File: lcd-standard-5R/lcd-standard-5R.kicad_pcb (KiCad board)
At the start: 2 copper layers, 137.4 x 82.6 mm, 114 parts, among them J1 SWD, J2 Conn_01x40_MountingPin, J3 Micro_SD_Card_Det1, J4 USB_C_Receptacle_USB2.0_16P, J5 Conn_01x06_MountingPin, J6 Serial, J7 Conn_ARM_JTAG_SWD_10, J8 Conn_01x02_MountingPin, J9 Conn_01x10_MountingPin, Q1 DMG2301L, Q2 MMBT3904, Q3 MMBT3904, Q4 MMBT3904, SW1 BOOT0, SW2 RST, U1 MAX98357A, U2 TPS61169, U3 XPT2046TS, U4 CAT24C256, U5 AMS1117-3.3, U6 siplex-som-s16

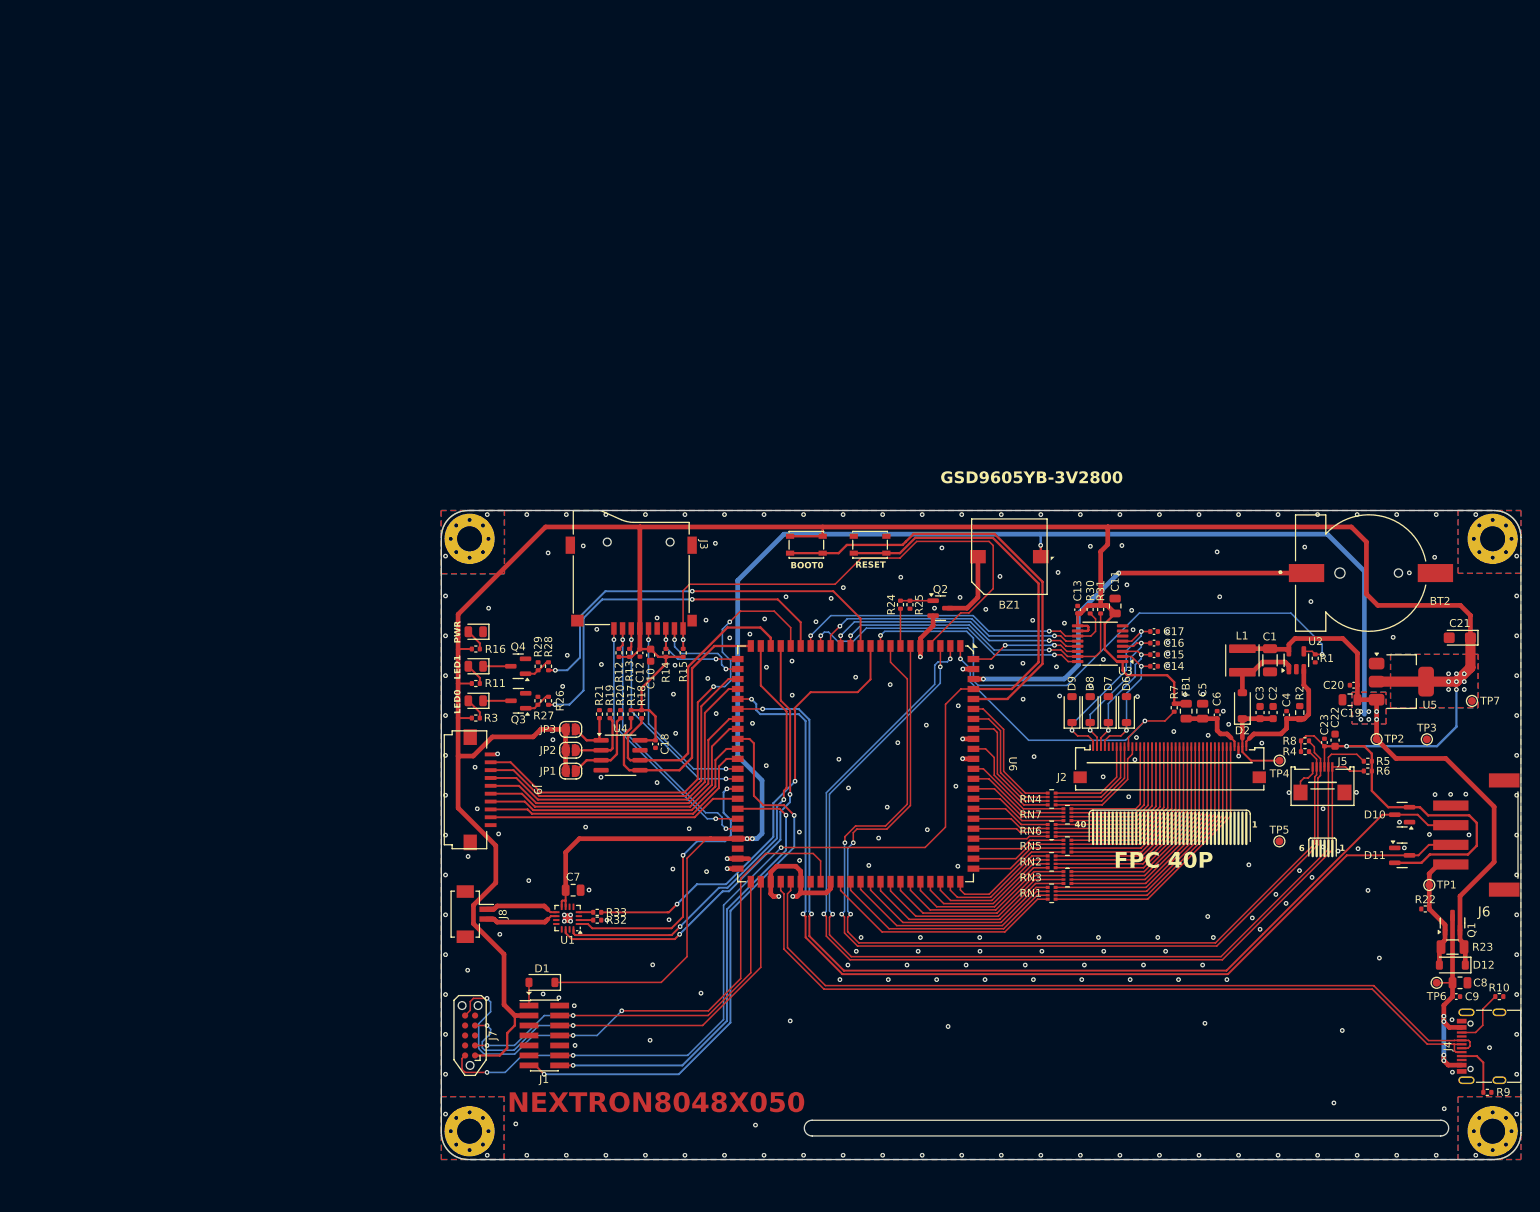
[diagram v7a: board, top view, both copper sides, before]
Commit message: Change LCD 5R to onboard MCU, cause separate boards are too expensive
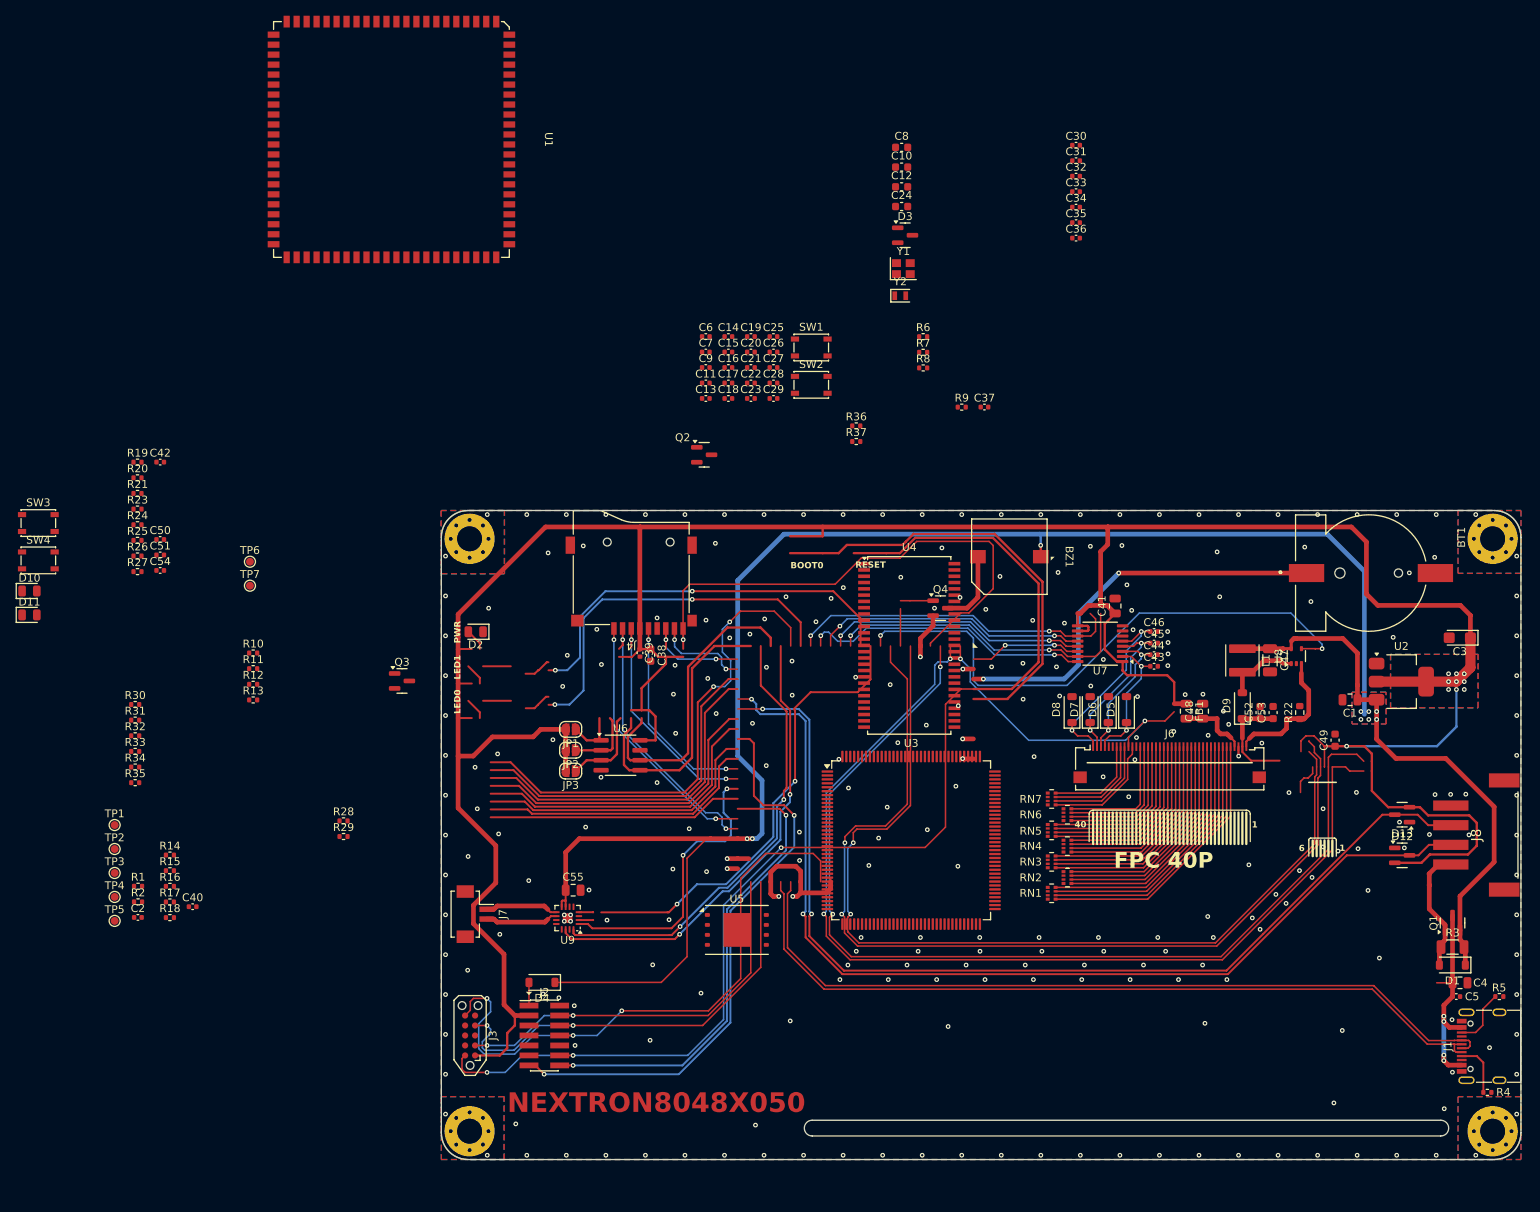
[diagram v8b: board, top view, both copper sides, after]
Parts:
- removed BT2: S8411-45R, CR1220-Batt-conn-S8411-45R:CR1220-Batt-conn-S8411-45R
- removed the C4 at (184.0, 79.9)
- removed the C5 at (173.3, 79.5)
- removed the J1 at (89.5, 120.7)
- removed J5: Conn_01x06_MountingPin, Connector_FPC:Conn_FPC_6P_0.5mm_XUNPU_FPC-05FB-6PH20
- removed J9: Conn_01x10_MountingPin, Connector_FPC:Conn_FPC_10P_1mm_G-SWITCH_GT-F1008SR20-10SMT01
- removed the R4 at (186.3, 84.6)
- removed the R5 at (194.3, 85.8)
- removed the U1 at (92.5, 105.8)
- added BT1: S8411-45R, CR1220-Batt-conn-S8411-45R:CR1220-Batt-conn-S8411-45R, F.Cu at (194.5, 61.9)
- added C24: 4u7, Capacitor_SMD:C_0603_1608Metric, F.Cu at (135.0, 15.2)
- added C25: 16p, Capacitor_SMD:C_0402_1005Metric, F.Cu at (118.7, 31.8)
- added C26: 16p, Capacitor_SMD:C_0402_1005Metric, F.Cu at (118.7, 33.7)
- added C27: 10p, Capacitor_SMD:C_0402_1005Metric, F.Cu at (118.7, 35.7)
- added C28: 10p, Capacitor_SMD:C_0402_1005Metric, F.Cu at (118.7, 37.7)
- added C29: 100n, Capacitor_SMD:C_0402_1005Metric, F.Cu at (118.7, 39.7)
- added C30: 100n, Capacitor_SMD:C_0402_1005Metric, F.Cu at (157.2, 7.43)
- added C31: 100n, Capacitor_SMD:C_0402_1005Metric, F.Cu at (157.2, 9.40)
- added C32: 100n, Capacitor_SMD:C_0402_1005Metric, F.Cu at (157.2, 11.4)
- added C33: 100n, Capacitor_SMD:C_0402_1005Metric, F.Cu at (157.2, 13.3)
- added C34: 100n, Capacitor_SMD:C_0402_1005Metric, F.Cu at (157.2, 15.3)
- added C35: 100n, Capacitor_SMD:C_0402_1005Metric, F.Cu at (157.2, 17.3)
- added C36: 100n, Capacitor_SMD:C_0402_1005Metric, F.Cu at (157.2, 19.2)
- added C37: 100n, Capacitor_SMD:C_0402_1005Metric, F.Cu at (145.5, 40.7)
- added C38: 1u, Capacitor_SMD:C_0603_1608Metric, F.Cu at (103.1, 72.3)
- added C39: 100n, Capacitor_SMD:C_0402_1005Metric, F.Cu at (101.7, 72.0)
- added C40: 100n, Capacitor_SMD:C_0402_1005Metric, F.Cu at (44.8, 104.3)
- added C41: 10u, Capacitor_SMD:C_0805_2012Metric, F.Cu at (162.2, 66.1)
- added C42: 100n, Capacitor_SMD:C_0402_1005Metric, F.Cu at (40.7, 47.8)
- added C43: 100n, Capacitor_SMD:C_0402_1005Metric, F.Cu at (167.1, 73.7)
- added C44: 100n, Capacitor_SMD:C_0402_1005Metric, F.Cu at (167.1, 72.3)
- added C45: 100n, Capacitor_SMD:C_0402_1005Metric, F.Cu at (167.1, 70.8)
- added C46: 100n, Capacitor_SMD:C_0402_1005Metric, F.Cu at (167.1, 69.3)
- added C47: 10u/1206, Capacitor_SMD:C_1206_3216Metric, F.Cu at (181.9, 73.0)
- added C48: 10u, Capacitor_SMD:C_0805_2012Metric, F.Cu at (173.3, 79.5)
- added C49: 1u, Capacitor_SMD:C_0603_1608Metric, F.Cu at (190.2, 83.1)
- added C50: 100n, Capacitor_SMD:C_0402_1005Metric, F.Cu at (40.7, 57.6)
- added C51: 100n, Capacitor_SMD:C_0402_1005Metric, F.Cu at (40.7, 59.6)
- added C52: 1u, Capacitor_SMD:C_0603_1608Metric, F.Cu at (180.6, 79.6)
- added C53: 1u, Capacitor_SMD:C_0603_1608Metric, F.Cu at (182.3, 79.6)
- added C54: 100n, Capacitor_SMD:C_0402_1005Metric, F.Cu at (40.7, 61.5)
- added C55: 10u, Capacitor_SMD:C_0805_2012Metric, F.Cu at (93.2, 102.2)
- added C8: 1u, Capacitor_SMD:C_0603_1608Metric, F.Cu at (135.0, 7.70)
- added C9: 100n, Capacitor_SMD:C_0402_1005Metric, F.Cu at (110.1, 35.7)
- added D13: BAT54S, Package_TO_SOT_SMD:SOT-23, F.Cu at (198.7, 92.6)
- added J4: Micro_SD_Card_Det1, TF-115:SD-TF-115, F.Cu at (100.6, 63.7)
- added R10: 10K, Resistor_SMD:R_0402_1005Metric, F.Cu at (52.5, 72.1)
- added R34: 10K, Resistor_SMD:R_0402_1005Metric, F.Cu at (37.5, 86.6)
- added R35: 2K, Resistor_SMD:R_0402_1005Metric, F.Cu at (37.5, 88.6)
- added R36: 1K, Resistor_SMD:R_0402_1005Metric, F.Cu at (129.2, 43.1)
- added R37: 10K, Resistor_SMD:R_0402_1005Metric, F.Cu at (129.2, 45.1)
- added R9: 10K, Resistor_SMD:R_0402_1005Metric, F.Cu at (142.7, 40.8)
- added SW3: BOOT0, Button_Switch_SMD:SW_SPST_PTS810, F.Cu at (25.1, 55.5)
- added SW4: RST, Button_Switch_SMD:SW_SPST_PTS810, F.Cu at (25.1, 60.3)
- added U6: CAT24C256, Package_SO:SOIC-8_3.9x4.9mm_P1.27mm, F.Cu at (99.2, 85.1)
- added U7: XPT2046TS, Package_SO:TSSOP-16_4.4x5mm_P0.65mm, F.Cu at (160.3, 70.9)
- added U8: TPS61169, Package_TO_SOT_SMD:SOT-353_SC-70-5, F.Cu at (185.2, 72.4)
- added U9: MAX98357A, Package_DFN_QFN:TQFN-16-1EP_3x3mm_P0.5mm_EP1.23x1.23mm, F.Cu at (92.5, 105.8)
- added Y1: 25MHz, Crystal:Crystal_SMD_2520-4Pin_2.5x2.0mm, F.Cu at (135.2, 23.1)
- added Y2: 32.768KHz, Crystal:Crystal_SMD_2012-2Pin_2.0x1.2mm, F.Cu at (134.8, 26.6)
- C1: value 10u/1206 -> 10u; footprint Capacitor_SMD:C_1206_3216Metric -> Capacitor_SMD:C_0805_2012Metric
- C10: value 1u -> 2u2
- C11, C19, C7: value 10u -> 100n; footprint Capacitor_SMD:C_0805_2012Metric -> Capacitor_SMD:C_0402_1005Metric
- C12: value 100n -> 2u2; footprint Capacitor_SMD:C_0402_1005Metric -> Capacitor_SMD:C_0603_1608Metric
- C2, C22: value 1u -> 100n; footprint Capacitor_SMD:C_0603_1608Metric -> Capacitor_SMD:C_0402_1005Metric
- C21: value 22uF -> 100n; footprint Capacitor_Tantalum_SMD:CP_EIA-3216-18_Kemet-A -> Capacitor_SMD:C_0402_1005Metric
- C3: value 1u -> 10uF; footprint Capacitor_SMD:C_0603_1608Metric -> Capacitor_Tantalum_SMD:CP_EIA-3216-18_Kemet-A
- D1: value NSR0320MW2T1G -> B5819W
- D10, D11: value BAT54S -> RED; footprint Package_TO_SOT_SMD:SOT-23 -> LED_SMD:LED_0805_2012Metric
- D12: value MBR0540 -> BAT54S; footprint Diode_SMD:D_SOD-123 -> Package_TO_SOT_SMD:SOT-23
- D2: value MBR0540 -> GREEN; footprint Diode_SMD:D_SOD-123 -> LED_SMD:LED_0805_2012Metric
- D3: value LED -> BAT54CW; footprint LED_SMD:LED_0805_2012Metric -> Package_TO_SOT_SMD:SOT-23
- D4: value LED -> B5819WS; footprint LED_SMD:LED_0805_2012Metric -> Diode_SMD:D_SOD-123
- D5: value LED -> MMSZ5226BT1G; footprint LED_SMD:LED_0805_2012Metric -> Diode_SMD:D_SOD-123
- D9: value MMSZ5226BT1G -> MBR0540
- J2: value Conn_01x40_MountingPin -> SWD; footprint Connector_FFC-FPC:Omron_XF2M-4015-1A_1x40-1MP_P0.5mm_Horizontal -> Connector_PinHeader_1.27mm:PinHeader_2x07_P1.27mm_Vertical_SMD
- J3: value Micro_SD_Card_Det1 -> Conn_ARM_JTAG_SWD_10; footprint TF-115:SD-TF-115 -> Connector:Tag-Connect_TC2050-IDC-NL_2x05_P1.27mm_Vertical
- J6: value Serial -> Conn_01x40_MountingPin; footprint S4B-XH-SM4-TB_LF__SN:S4BXHSM4TBLFSN -> Connector_FFC-FPC:Omron_XF2M-4015-1A_1x40-1MP_P0.5mm_Horizontal
- J7: value Conn_ARM_JTAG_SWD_10 -> Conn_01x02_MountingPin; footprint Connector:Tag-Connect_TC2050-IDC-NL_2x05_P1.27mm_Vertical -> Connector_Hirose:Hirose_DF13C_CL535-0402-2-51_1x02-1MP_P1.25mm_Vertical
- J8: value Conn_01x02_MountingPin -> Serial; footprint Connector_Hirose:Hirose_DF13C_CL535-0402-2-51_1x02-1MP_P1.25mm_Vertical -> S4B-XH-SM4-TB_LF__SN:S4BXHSM4TBLFSN
- L1: value 6.8u -> 4.7u
- Q1: value DMG2301L -> DMG3415
- R11: value 2K -> 10K
- R14, R15, R25: value 10K -> 2K2
- R16: value 2K -> 2K2
- R19, R20, R21, R6: value 2K2 -> 10K
- R2: value 4.7R -> 2K; footprint Resistor_SMD:R_0603_1608Metric -> Resistor_SMD:R_0402_1005Metric
- R22: value 10K -> 4.7R; footprint Resistor_SMD:R_0402_1005Metric -> Resistor_SMD:R_0603_1608Metric
- R23: value 0 -> 10K; footprint Resistor_SMD:R_1206_3216Metric -> Resistor_SMD:R_0402_1005Metric
- R24: value 1K -> 10K
- R26: value 1K -> 2K2
- R28: value 1K -> 1M
- R29: value 10K -> 100K
- R3: value 2K -> 0; footprint Resistor_SMD:R_0402_1005Metric -> Resistor_SMD:R_1206_3216Metric
- R30: value 10K -> 1K
- R32: value 100K -> 2K
- R33: value 1M -> 1K
- SW1: value BOOT0 -> SW_Push
- SW2: value RST -> SW_Push
- U2: value TPS61169 -> AMS1117-3.3; footprint Package_TO_SOT_SMD:SOT-23-5 -> Package_TO_SOT_SMD:SOT-223-3_TabPin2
- U3: value XPT2046TS -> STM32H743ZITx; footprint Package_SO:TSSOP-16_4.4x5mm_P0.65mm -> Package_QFP:LQFP-144_20x20mm_P0.5mm
- U4: value CAT24C256 -> MT48LC16M16A2P; footprint Package_SO:SOIC-8_3.9x4.9mm_P1.27mm -> Package_SO:TSOP-II-54_22.2x10.16mm_P0.8mm
- U5: value AMS1117-3.3 -> MT25Q; footprint Package_TO_SOT_SMD:SOT-223-3_TabPin2 -> Package_SON:WSON-8-1EP_8x6mm_P1.27mm_EP3.4x4.3mm
- moved D11 177.4 mm to (24.0, 67.2)
- moved D10 177.0 mm to (24.0, 64.2), turned to 0 degrees
- moved R23 176.4 mm to (37.8, 53.7)
- moved TP3 167.9 mm to (34.9, 100.0)
- moved TP1 167.5 mm to (34.9, 93.9)
- moved TP2 161.2 mm to (34.9, 97.0)
- moved TP6 160.3 mm to (52.1, 60.4)
- moved TP7 156.2 mm to (52.1, 63.5)
- moved R1 152.6 mm to (37.8, 101.7), turned to 0 degrees
- moved R2 149.8 mm to (37.8, 103.7), turned to 0 degrees
- moved TP4 149.3 mm to (34.9, 103.1)
- moved TP5 148.6 mm to (34.9, 106.1)
- moved C2 146.8 mm to (37.8, 105.7), turned to 0 degrees
- moved J8 128.8 mm to (209.2, 95.2), turned to 90 degrees
- moved R3 127.7 mm to (205.1, 109.5), turned to 0 degrees
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- renumbered C8 to C4, C9 to C5, J4 to J1, R9 to R4, R10 to R5, RN3 to RN2, RN2 to RN3, RN5 to RN4, RN6 to RN5, RN7 to RN6, RN4 to RN7, U6 to U1
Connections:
- C10 pad 1: +3V3 -> Net-(C10-Pad1)
- C12 pad 1: +3V3 -> Net-(C10-Pad1)
- C13 pad 1: +3V3 -> VBAT
- C14 pad 1: /XR -> +3V3
- C15 pad 1: /YD -> +3V3
- C16 pad 1: /XL -> +3V3
- C17 pad 1: /YU -> +3V3
- C19 pad 1: VDD -> +3V3
- C2 pad 1: /LED_A -> VDD
- C20 pad 1: VDD -> +3V3
- C3 pad 1: /LED_A -> +3V3
- C6 pad 1: VDD_LCD -> +3V3
- C7 pad 1: VDD -> +3V3
- D1 pad 2: Net-(D1-A) -> VEXT
- D10 pad 1: GND -> Net-(D10-K)
- D10 pad 2: +3V3 -> Net-(D10-A)
- D11 pad 1: GND -> Net-(D11-K)
- D11 pad 2: +3V3 -> Net-(D11-A)
- D12 pad 1: VDD -> GND
- D12 pad 2: VEXT -> +3V3
- D2 pad 1: /LED_A -> GND
- D2 pad 2: /SW -> Net-(D2-A)
- D3 pad 1: Net-(D3-K) -> VB
- D3 pad 2: Net-(D3-A) -> +3V3
- D4 pad 1: Net-(D4-K) -> VDD
- D5 pad 1: GND -> /DISPLAY/XR
- D5 pad 2: Net-(D5-A) -> GND
- D6 pad 1: /XR -> /DISPLAY/YD
- D7 pad 1: /YD -> /DISPLAY/XL
- D8 pad 1: /XL -> /DISPLAY/YU
- D9 pad 1: /YU -> /DISPLAY/LED_A
- D9 pad 2: GND -> /DISPLAY/SW
- J2 pad 1: /YU -> Net-(D4-A)
- J2 pad 10: /LCD_RST -> unconnected-(J2-Pin_10-Pad10)
- J2 pad 11: /LCD_CLK -> unconnected-(J2-Pin_11-Pad11)
- J2 pad 12: GND -> /MCU/RESET
- J2 pad 13: /LCD_B7 -> /MCU/DBG_RX
- J2 pad 14: /LCD_B6 -> /MCU/DBG_TX
- J2 pad 2: /XL -> GND
- J2 pad 3: /YD -> +3V3
- J2 pad 4: /XR -> /MCU/SWDIO
- J2 pad 6: unconnected-(J2-Pin_6-Pad6) -> /MCU/SWCLK
- J2 pad 7: /LCD_DE -> GND
- J2 pad 8: /LCD_VSYNC -> /MCU/SWO
- J2 pad 9: /LCD_HSYNC -> unconnected-(J2-Pin_9-Pad9)
- J3 pad 1: /DAT2 -> +3V3
- J3 pad 10: GND -> /MCU/RESET
- J3 pad 2: /DAT3 -> /MCU/SWDIO
- J3 pad 3: /CMD -> GND
- J3 pad 4: +3V3 -> /MCU/SWCLK
- J3 pad 5: /CLK -> GND
- J3 pad 6: GND -> /MCU/SWO
- J3 pad 7: /DAT0 -> unconnected-(J3-KEY-Pad7)
- J3 pad 8: /DAT1 -> unconnected-(J3-NC/TDI-Pad8)
- J3 pad 9: /SD_DET -> unconnected-(J3-GNDDetect-Pad9)
- J6 pad 1: VEXT -> /DISPLAY/YU
- J6 pad 2: /SERIAL_TX -> /DISPLAY/XL
- J6 pad 3: /SERIAL_RX -> /DISPLAY/YD
- J6 pad 4: GND -> /DISPLAY/XR
- J7 pad 1: +3V3 -> Net-(J7-Pin_1)
- J7 pad 2: /SWDIO -> Net-(J7-Pin_2)
- J8 pad 1: Net-(J8-Pin_1) -> VEXT
- J8 pad 2: Net-(J8-Pin_2) -> /IO/SERIAL_TX
- L1 pad 2: /SW -> /DISPLAY/SW
- Q2 pad 3: Net-(BZ1--) -> Net-(D10-K)
- Q3 pad 3: Net-(D3-K) -> Net-(D11-K)
- Q4 pad 3: Net-(D4-K) -> Net-(BZ1--)
- R1 pad 1: /LCD_BLK -> VEXT
- R11 pad 1: Net-(D4-A) -> +3V3
- R11 pad 2: +3V3 -> /MEMORY_SD_CARD/DAT0
- R12 pad 2: /DAT3 -> /MEMORY_SD_CARD/CMD
- R13 pad 2: /CMD -> /MEMORY_SD_CARD/DAT3
- R14 pad 1: +3V3 -> Net-(JP1-A)
- R14 pad 2: /DAT0 -> GND
- R15 pad 1: +3V3 -> Net-(JP2-A)
- R15 pad 2: /SD_DET -> GND
- R16 pad 1: +3V3 -> Net-(JP3-A)
- R16 pad 2: Net-(D5-A) -> GND
- R17 pad 2: /EE_SDA -> /MEMORY_EEPROM/EE_SDA
- R18 pad 2: /EE_SCL -> /MEMORY_EEPROM/EE_SCL
- R19 pad 1: Net-(JP2-A) -> +3V3
- R19 pad 2: GND -> /DISPLAY/TP_CS
- R2 pad 1: /LED_K -> +3V3
- R2 pad 2: GND -> Net-(D2-A)
- R20 pad 1: Net-(JP1-A) -> +3V3
- R20 pad 2: GND -> /DISPLAY/TP_IRQ
- R21 pad 1: Net-(JP3-A) -> /DISPLAY/LCD_BLK
- R22 pad 1: VEXT -> /DISPLAY/LED_K
- R23 pad 1: VEXT -> /DISPLAY/TP_INT
- R23 pad 2: VDD -> +3V3
- R24 pad 1: /BUZZER -> /DISPLAY/TP_WAKE
- R24 pad 2: Net-(Q2-B) -> +3V3
- R25 pad 1: Net-(Q2-B) -> +3V3
- R25 pad 2: GND -> /DISPLAY/TP_SDA
- R26 pad 1: /LED0 -> +3V3
- R26 pad 2: Net-(Q3-B) -> /DISPLAY/TP_SCL
- R27 pad 1: Net-(Q3-B) -> +3V3
- R27 pad 2: GND -> /DISPLAY/LCD_RST
- R28 pad 1: /LED1 -> Net-(U9-~{SD_MODE})
- R28 pad 2: Net-(Q4-B) -> /OUTPUT_SPEAKER/~{SD_MODE}
- R29 pad 1: Net-(Q4-B) -> /OUTPUT_SPEAKER/GAIN_SLOT
- R3 pad 1: Net-(D3-A) -> VEXT
- R3 pad 2: +3V3 -> VDD
- R30 pad 1: +3V3 -> /IO/LED0
- R30 pad 2: /TP_IRQ -> Net-(Q2-B)
- R31 pad 1: +3V3 -> Net-(Q2-B)
- R31 pad 2: /TP_CS -> GND
- R32 pad 1: /GAIN_SLOT -> Net-(D10-A)
- R32 pad 2: GND -> +3V3
- R33 pad 1: Net-(U1-~{SD_MODE}) -> /IO/LED1
- R33 pad 2: /~{SD_MODE} -> Net-(Q3-B)
- R6 pad 2: /TP_SCL -> Net-(U3-PDR_ON)
- R7 pad 2: /LCD_RST -> /MCU/NRST
- R8 pad 1: /TP_WAKE -> /MCU/BOOT0
- R8 pad 2: +3V3 -> GND
- SW1 pad 1: /BOOT0 -> /MCU/BOOT0
- SW2 pad 1: /RESET -> /MCU/NRST
- TP1 pad 1: VEXT -> VBUS
- TP2 pad 1: VDD -> VEXT
- TP4 pad 1: /LED_A -> VDD
- TP5 pad 1: GND -> +3V3
- TP6 pad 1: VBUS -> /DISPLAY/LED_A
- TP7 pad 1: +3V3 -> GND
- U2 pad 1: /SW -> GND
- U2 pad 2: GND -> +3V3
- U2 pad 3: /LED_K -> VDD
- U3 pad 1: +3V3 -> /MCU/LCS_SPI_CLK
- U3 pad 10: +3V3 -> /MCU/SDRAM_ADD0
- U3 pad 11: /TP_IRQ -> /MCU/SDRAM_ADD1
- U3 pad 12: /TP_MISO -> /MCU/SDRAM_ADD2
- U3 pad 13: /TP_BUSY -> /MCU/SDRAM_ADD3
- U3 pad 14: /TP_MOSI -> /MCU/SDRAM_ADD4
- U3 pad 15: /TP_CS -> /MCU/SDRAM_ADD5
- U3 pad 16: /TP_CLK -> GND
- U3 pad 2: /XR -> /MCU/LCS_SPI_CS
- U3 pad 3: /YD -> /MCU/LCD_RESET
- U3 pad 4: /XL -> unconnected-(U3-PE5-Pad4)
- U3 pad 5: /YU -> /MCU/LCS_SPI_DAT
- U3 pad 6: GND -> VBAT
- U3 pad 8: unconnected-(U3-IN-Pad8) -> /MCU/OSC32_IN
- U3 pad 9: +3V3 -> /MCU/OSC32_OUT
- U4 pad 1: Net-(JP3-A) -> +3V3
- U4 pad 2: Net-(JP2-A) -> /MEMORY_FMC/SDRAM_DQ0
- U4 pad 3: Net-(JP1-A) -> +3V3
- U4 pad 4: GND -> /MEMORY_FMC/SDRAM_DQ1
- U4 pad 5: /EE_SDA -> /MEMORY_FMC/SDRAM_DQ2
- U4 pad 6: /EE_SCL -> GND
- U4 pad 7: GND -> /MEMORY_FMC/SDRAM_DQ3
- U4 pad 8: +3V3 -> /MEMORY_FMC/SDRAM_DQ4
- U5 pad 1: GND -> /MEMORY_FLASH/~{NOR_CS}
- U5 pad 2: +3V3 -> /MEMORY_FLASH/NOR_DO(IO1)
- U5 pad 3: VDD -> /MEMORY_FLASH/NOR_IO2
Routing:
- net /SERIAL_RX: track 129.7 -> 0.00 mm, vias 2 -> 0
- net /IO/SERIAL_RX: track 0.00 -> 129.7 mm, vias 0 -> 2
- net /SERIAL_TX: track 128.9 -> 0.00 mm, vias 2 -> 0
- net /IO/SERIAL_TX: track 0.00 -> 128.9 mm, vias 0 -> 2
- net /MEMORY_FMC/SDRAM_UDQM: track 0.00 -> 88.1 mm
- net /MEMORY_FMC/SDRAM_CLK: track 0.00 -> 79.1 mm
- net /SWO: track 78.2 -> 0.00 mm, vias 3 -> 0
- net /MCU/SWO: track 0.00 -> 78.2 mm, vias 0 -> 3
- net /MCU/DBG_RX: track 0.00 -> 73.7 mm, vias 0 -> 2
- net /DBG_RX: track 73.7 -> 0.00 mm, vias 2 -> 0
- net /LCD_BLK: track 73.0 -> 0.00 mm, vias 2 -> 0
- net /DISPLAY/LCD_BLK: track 0.00 -> 72.4 mm, vias 0 -> 2
- net /SD_DET: track 66.4 -> 0.00 mm, vias 1 -> 0
- net /MEMORY_SD_CARD/SD_DET: track 0.00 -> 66.4 mm, vias 0 -> 1
- net unconnected-(U4-NC-Pad40): track 0.00 -> 63.6 mm, vias 0 -> 2
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- added copper zone on In2.Cu, net +3V3
- added copper zone on In1.Cu, net GND
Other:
- copper layers 2 -> 4
